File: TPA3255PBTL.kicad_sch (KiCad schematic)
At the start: 37 parts, among them Q2 DMN10H220L, Q3 DMN10H220L, SW1 SW_Push_Dual, U1 TPA3255DDV

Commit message: pre fab-no heatsink
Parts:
- removed C14: 100n, Capacitor_SMD:C_0805_2012Metric, symbol Device:C
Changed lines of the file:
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@@
   (junction (at 201.93 91.44) (diameter 0) (color 0 0 0 0)
   )
-  (junction (at 27.94 85.09) (diameter 0) (color 0 0 0 0)
-  )
   (junction (at 157.48 147.32) (diameter 0) (color 0 0 0 0)
   )
@@
   (junction (at 85.09 66.04) (diameter 0) (color 0 0 0 0)
   )
-  (junction (at 27.94 97.79) (diameter 0) (color 0 0 0 0)
-  )
   (junction (at 48.26 128.27) (diameter 0) (color 0 0 0 0)
   )
@@
     (stroke (width 0) (type default) (color 0 0 0 0))
   )
-  (wire (pts (xy 27.94 96.52) (xy 27.94 97.79))
+  (wire (pts (xy 27.94 96.52) (xy 27.94 99.06))
     (stroke (width 0) (type default) (color 0 0 0 0))
   )
@@
     (stroke (width 0) (type default) (color 0 0 0 0))
   )
-  (wire (pts (xy 35.56 97.79) (xy 27.94 97.79))
-    (stroke (width 0) (type default) (color 0 0 0 0))
-  )
   (wire (pts (xy 109.22 68.58) (xy 85.09 68.58))
     (stroke (width 0) (type default) (color 0 0 0 0))
@@
     (stroke (width 0) (type default) (color 0 0 0 0))
   )
-  (wire (pts (xy 35.56 88.9) (xy 35.56 85.09))
-    (stroke (width 0) (type default) (color 0 0 0 0))
-  )
   (wire (pts (xy 106.68 190.5) (xy 106.68 191.77))
     (stroke (width 0) (type default) (color 0 0 0 0))
@@
     (stroke (width 0) (type default) (color 0 0 0 0))
   )
-  (wire (pts (xy 27.94 97.79) (xy 27.94 99.06))
-    (stroke (width 0) (type default) (color 0 0 0 0))
-  )
   (wire (pts (xy 110.49 29.21) (xy 110.49 30.48))
     (stroke (width 0) (type default) (color 0 0 0 0))
@@
     (stroke (width 0) (type default) (color 0 0 0 0))
   )
-  (wire (pts (xy 35.56 96.52) (xy 35.56 97.79))
-    (stroke (width 0) (type default) (color 0 0 0 0))
-  )
   (wire (pts (xy 156.21 91.44) (xy 154.94 91.44))
     (stroke (width 0) (type default) (color 0 0 0 0))
@@
   )
   (wire (pts (xy 110.49 20.32) (xy 114.3 20.32))
-    (stroke (width 0) (type default) (color 0 0 0 0))
-  )
-  (wire (pts (xy 35.56 85.09) (xy 27.94 85.09))
     (stroke (width 0) (type default) (color 0 0 0 0))
   )
@@
     (pin "2")
   )
-  (symbol (lib_id "Device:C") (at 35.56 92.71 0) (unit 1)
-    (in_bom yes) (on_board yes)
-    (property "Reference" "C14" (id 0) (at 38.481 91.8015 90)
-      (effects (font (size 1.27 1.27)) (justify left))
-    )
-    (property "Value" "100n" (id 1) (at 38.481 94.5766 0)
-      (effects (font (size 1.27 1.27)) (justify left))
-    )
-    (property "Footprint" "Capacitor_SMD:C_0805_2012Metric" (id 2) (at 36.5252 96.52 0)
-      (effects (font (size 1.27 1.27)) hide)
-    )
-    (property "Datasheet" "~" (id 3) (at 35.56 92.71 0)
-      (effects (font (size 1.27 1.27)) hide)
-    )
-    (pin "1")
-    (pin "2")
-  )
   (symbol (lib_id "Device:L") (at 182.88 110.49 90) (unit 1)
     (in_bom yes) (on_board yes) (fields_autoplaced)
@@
       (reference "C13") (unit 1) (value "1u") (footprint "Capacitor_SMD:C_0805_2012Metric")
     )
-    (path "/9dff25c6-72ff-4865-ac3b-964c164bd882"
-      (reference "C14") (unit 1) (value "100n") (footprint "Capacitor_SMD:C_0805_2012Metric")
-    )
     (path "/31a691eb-5a3f-4a88-af24-c08065fcede2/9dde5ae0-8e98-4968-855d-b711591decae"

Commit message: Update, Post mfg
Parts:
- removed C38, C39: 4.7n, Capacitor_THT:C_Rect_L18.0mm_W6.0mm_P15.00mm_FKS3_FKP3, symbol Device:C
- removed D5, D6: LED, LED_THT:LED_D3.0mm_Horizontal_O1.27mm_Z2.0mm, symbol Device:LED
- removed SW1: SW_Push_Dual, Button_Switch_SMD:SW_SPST_Omron_B3FS-105xP, symbol Switch:SW_Push_Dual
- added C14, C17: 1u, Capacitor_THT:C_Rect_L7.2mm_W7.2mm_P5.00mm_FKS2_FKP2_MKS2_MKP2, symbol Device:C
- added C18, C19: 1n, Capacitor_SMD:C_0805_2012Metric, symbol Device:C
- added C20, C27: 10n, Capacitor_SMD:C_0805_2012Metric, symbol Device:C
- added D5: LED_Dual_KAKA, Eli_Lib:IC4_WP934EB_2GD_KNB, symbol Device:LED_Dual_KAKA
- added L4, L5, L6, L7: 10u, Inductor_THT:L_Toroid_Vertical_L22.4mm_W10.2mm_P7.90mm_Vishay_TJ4, symbol Device:L
- added R10, R8: 3R3, Resistor_SMD:R_0805_2012Metric, symbol Device:R
- added TP1, TP5: TestPoint, TestPoint:TestPoint_THTPad_1.0x1.0mm_Drill0.5mm, symbol Connector:TestPoint
- C36, C37: value 220n -> 12n; footprint Capacitor_THT:C_Rect_L33.0mm_W20.0mm_P27.50mm_MKS4 -> Capacitor_SMD:C_0805_2012Metric
- C42: value 100n -> 47n
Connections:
- net Fault: now also TP1.1
- net GND: now also C14.2, C17.1, C18.2, C19.1, D5.1 (A1), D5.3 (A2), R10.2, R8.1
- net Load1: now also L4.2, L6.2; no longer C36.1, L2.2
- net Load2: now also L5.2, L7.1; no longer C37.2, L3.2
- net RST_: now also TP5.1
- net at Q3.3 (D), R28.1: now also D5.2 (K1)
- net at Q2.3 (D), R25.1: now also D5.4 (K2)
- new net: C36.1, L6.1
- new net: C37.2, L7.2
- new net: C20.2, R8.2
- new net: C27.1, R10.1
- new net OUTA2: C14.1, C18.1, C20.1, L2.2, L4.1
- new net OUTB2: C17.2, C19.2, C27.2, L3.2, L5.1
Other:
- added sheet StartupRst (StartupRst.kicad_sch)
- note added: "B32529D1105J289"
- note added: "Heatsink: ATS-TI1OP-519-C1-R3"
- note added: "SRP6060FA-100M"

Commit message: Pre mfg, Rev B
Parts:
- removed L6, L7: 10u, Inductor_THT:L_Toroid_Vertical_L22.4mm_W10.2mm_P7.90mm_Vishay_TJ4, symbol Device:L
- added C11, C8: 1u, Capacitor_THT:C_Rect_L7.2mm_W7.2mm_P5.00mm_FKS2_FKP2_MKS2_MKP2, symbol Device:C
- added J6: AC3MAH-AU-PRE, AC3MAH-AU-PRE_AMP, symbol Eli_v6Lib:AC3MAH-AU-PRE
- C36, C37: value 12n -> 1u; footprint Capacitor_SMD:C_0805_2012Metric -> Capacitor_THT:C_Rect_L7.2mm_W7.2mm_P5.00mm_FKS2_FKP2_MKS2_MKP2
- L4, L5: value 10u -> 22u
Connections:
- net GND: now also C11.1, J6.1, J6.G; no longer C37.1
- net Load1: now also C8.1, J6.3
- net Load2: now also C37.2, J6.2
- net at C36.1: now also C8.2
- new net: C11.2, C37.1

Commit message: minor changes
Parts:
- added TP7, TP8: TestPoint, TestPoint:TestPoint_THTPad_1.0x1.0mm_Drill0.5mm, symbol Connector:TestPoint
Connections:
- net GND: now also TP7.1, TP8.1

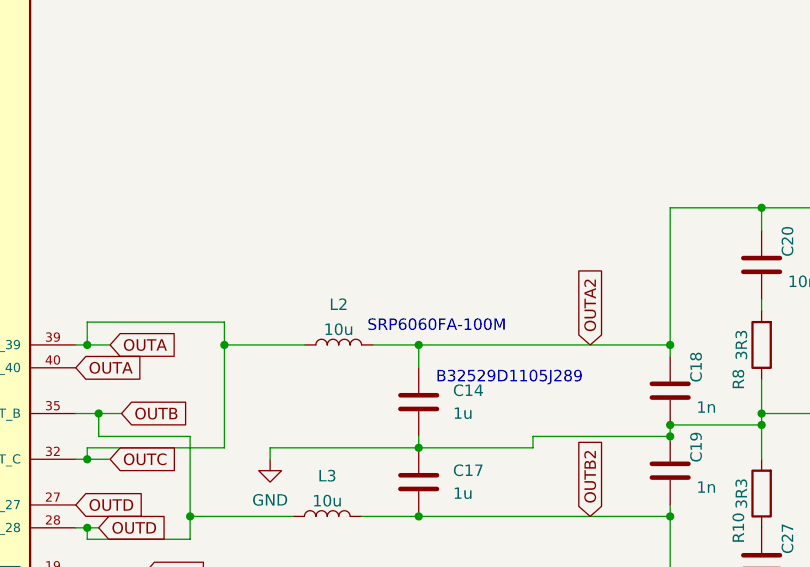
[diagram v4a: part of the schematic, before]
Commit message: Add testing/ update README/ Current control
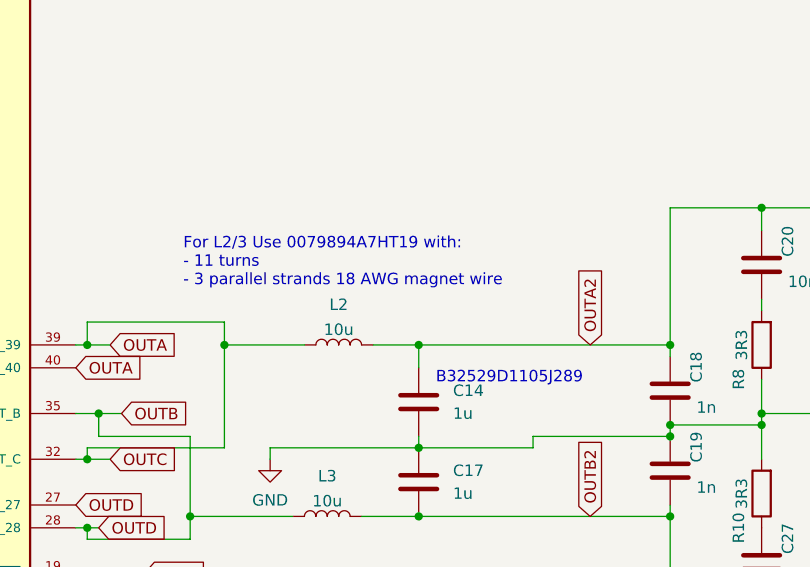
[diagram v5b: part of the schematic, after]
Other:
- note added: "For L2/3 Use 0079894A7HT19 with: - 11 turns - 3 parallel strands 18 AWG magnet wire"
- note removed: "SRP6060FA-100M"
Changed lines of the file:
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@@
 		)
 	)
-	(text "SRP6060FA-100M"
+	(text "For L2/3 Use 0079894A7HT19 with:\n- 11 turns\n- 3 parallel strands 18 AWG magnet wire"
 		(exclude_from_sim no)
-		(at 187.325 90.17 0)
+		(at 166.878 85.09 0)
 		(effects
 			(font
